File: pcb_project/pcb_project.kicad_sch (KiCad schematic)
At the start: 15 parts, among them J6 Conn_01x10_Pin

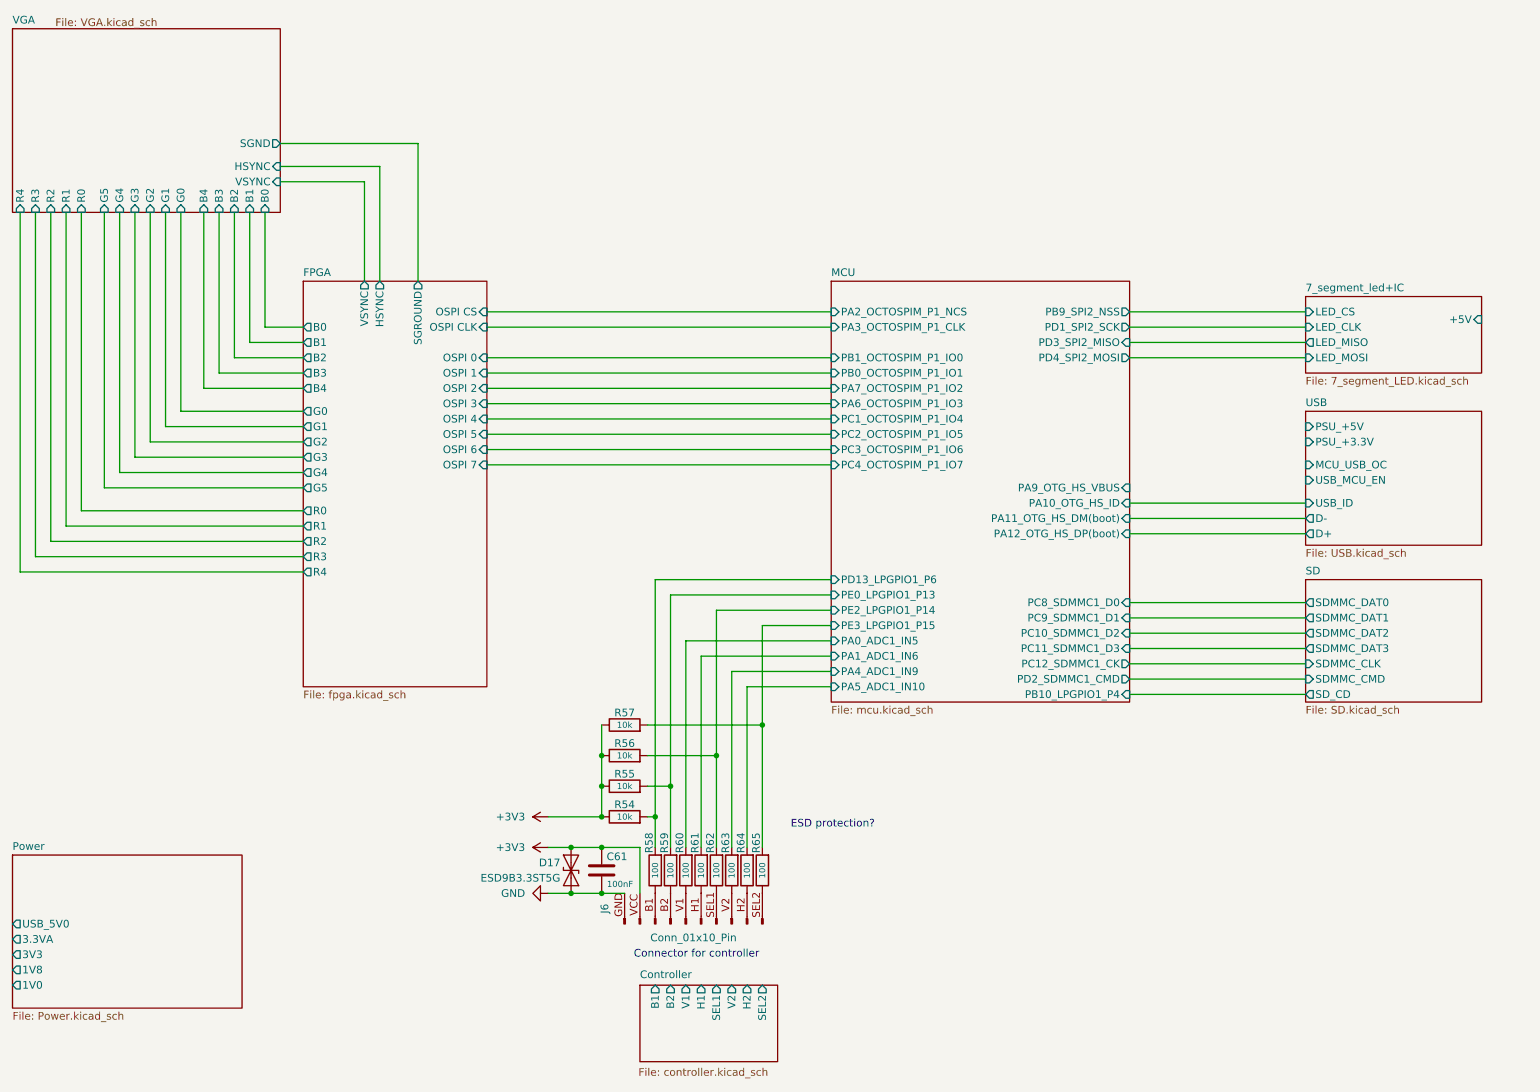
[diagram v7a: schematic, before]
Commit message: ERC fixes, some remain
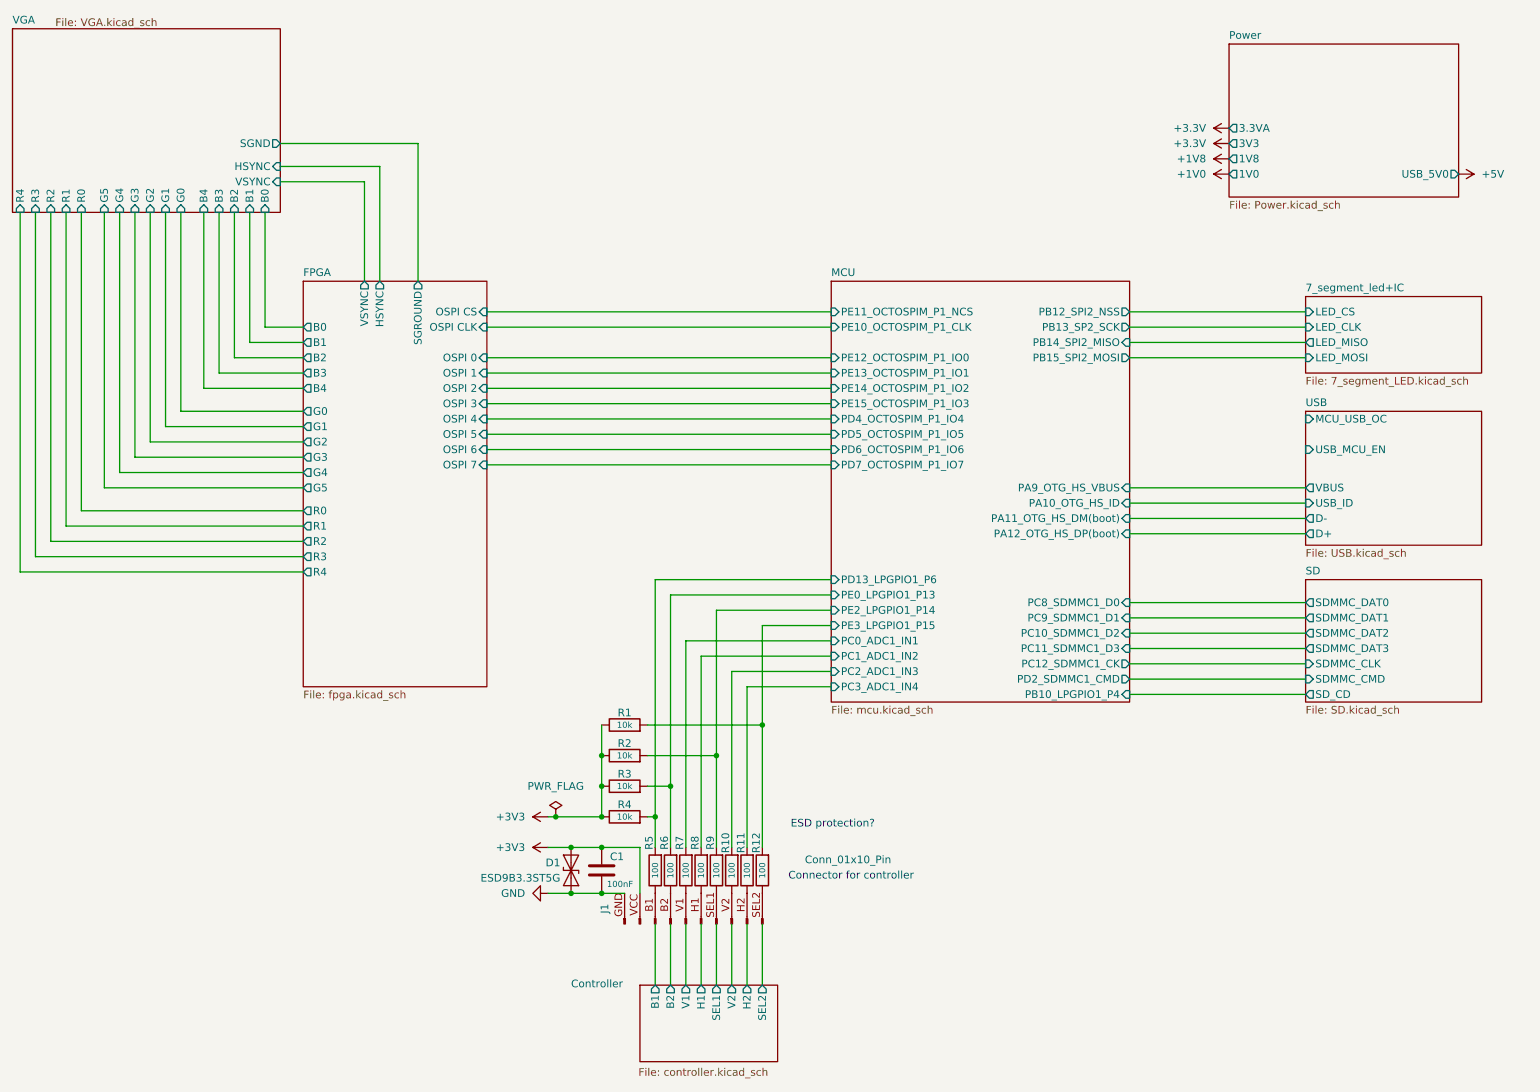
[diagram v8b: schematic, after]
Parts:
- renumbered C61 to C1, D17 to D1, J6 to J1, R57 to R1, R63 to R10, R64 to R11, R65 to R12, R56 to R2, R55 to R3, R54 to R4, R58 to R5, R59 to R6, R60 to R7, R61 to R8, R62 to R9
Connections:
- net MCU/PA0_ADC1_IN5 renamed MCU/PC0_ADC1_IN1
- net MCU/PA1_ADC1_IN6 renamed MCU/PC1_ADC1_IN2
- net MCU/PA4_ADC1_IN9 renamed MCU/PC2_ADC1_IN3
- net MCU/PA5_ADC1_IN10 renamed MCU/PC3_ADC1_IN4
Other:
- sheet 7_segment_led+IC ports: added none; removed +5V
- sheet MCU ports: added PB12_SPI2_NSS, PB13_SP2_SCK, PB14_SPI2_MISO, PB15_SPI2_MOSI, PC0_ADC1_IN1, PC1_ADC1_IN2, PC2_ADC1_IN3, PC3_ADC1_IN4, PD4_OCTOSPIM_P1_IO4, PD5_OCTOSPIM_P1_IO5, PD6_OCTOSPIM_P1_IO6, PD7_OCTOSPIM_P1_IO7, PE10_OCTOSPIM_P1_CLK, PE11_OCTOSPIM_P1_NCS, PE12_OCTOSPIM_P1_IO0, PE13_OCTOSPIM_P1_IO1, PE14_OCTOSPIM_P1_IO2, PE15_OCTOSPIM_P1_IO3; removed PA0_ADC1_IN5, PA1_ADC1_IN6, PA2_OCTOSPIM_P1_NCS, PA3_OCTOSPIM_P1_CLK, PA4_ADC1_IN9, PA5_ADC1_IN10, PA6_OCTOSPIM_P1_IO3, PA7_OCTOSPIM_P1_IO2, PB0_OCTOSPIM_P1_IO1, PB1_OCTOSPIM_P1_IO0, PB9_SPI2_NSS, PC1_OCTOSPIM_P1_IO4, PC2_OCTOSPIM_P1_IO5, PC3_OCTOSPIM_P1_IO6, PC4_OCTOSPIM_P1_IO7, PD1_SPI2_SCK, PD3_SPI2_MISO, PD4_SPI2_MOSI
- sheet USB ports: added VBUS; removed PSU_+3.3V, PSU_+5V
